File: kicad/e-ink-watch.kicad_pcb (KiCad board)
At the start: 4 copper layers, 40 x 40 mm, 42 parts, among them SW1 BTN1, SW2 BTN2, SW3 BTN3, U1 MDBT50Q-1MV2, U2 BQ25120A

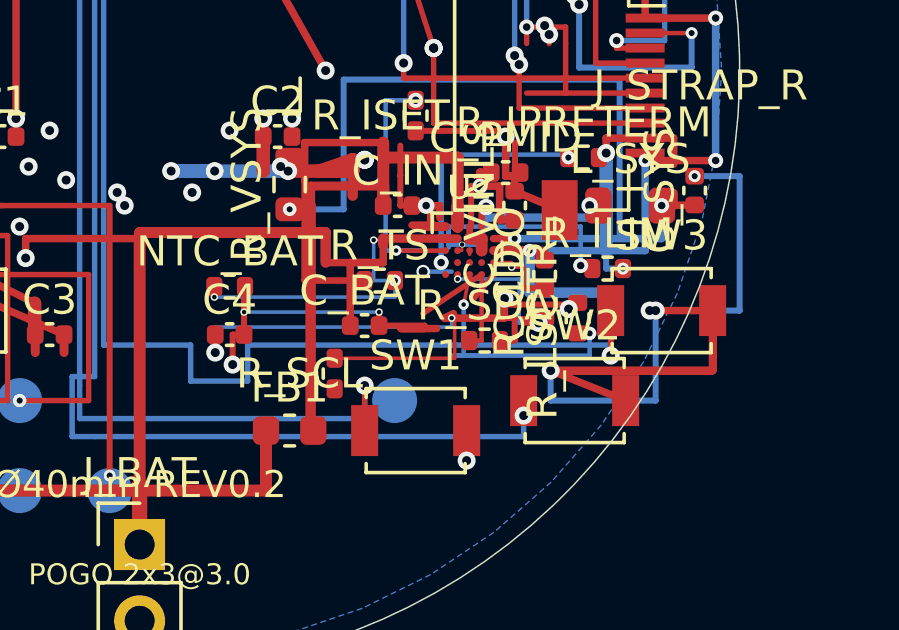
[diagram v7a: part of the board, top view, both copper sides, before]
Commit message: Slide R_SDA north off the SW2 courtyard.
Retract the 3V3 L vertical onto the existing via at x=110.4 so R_SDA can move to y=108.85 without the pad1-vs-3V3 short. Courtyard vs SW2 −0.120 → +0.030. West-of-VBUS SDA hops still hit the TS via drops. Shorting stays 0, unconnected stays 8.

Co-authored-by: illiapliukhin <illiapliukhin@users.noreply.github.com>
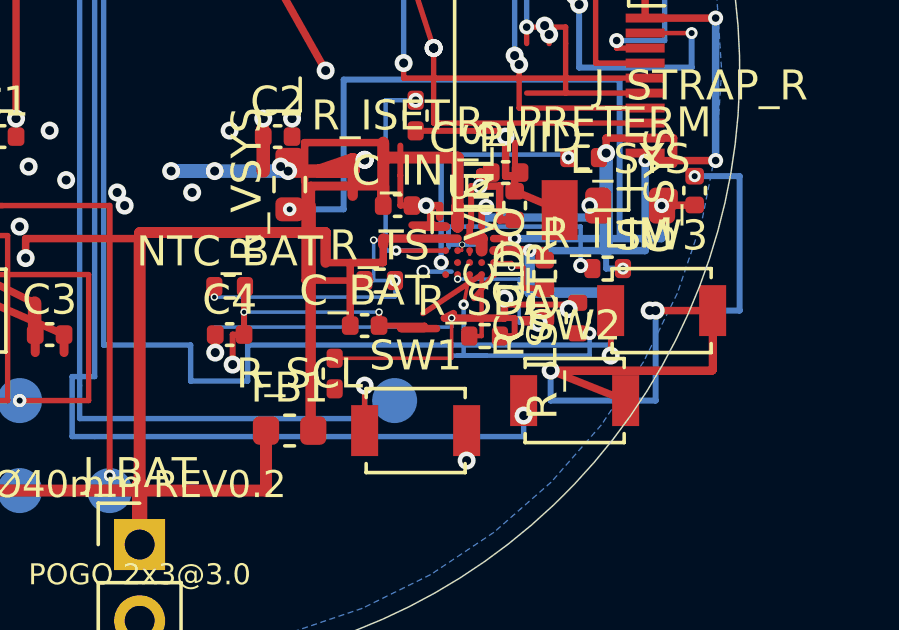
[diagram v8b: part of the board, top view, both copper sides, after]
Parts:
- moved R_SDA 0.15 mm to (111.5, 108.8)
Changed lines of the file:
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@@
 	(footprint "Resistor_SMD:R_0402_1005Metric"
 		(layer "F.Cu")
-		(at 111.5 109.0)
+		(at 111.5 108.85)
 		(descr "Resistor SMD 0402 (1005 Metric), square (rectangular) end terminal, IPC-7351 nominal, (Body size source: IPC-SM-782 page 72, https://www.pcb-3d.com/wordpress/wp-content/uploads/ipc-sm-782a_amendment_1_and_2.pdf), generated with kicad-footprint-generator")
 		(tags "resistor")
@@
 	)
 	(segment
-		(start 110.99 109.0)
-		(end 111.4 109.0)
+		(start 110.99 108.85)
+		(end 111.4 108.85)
 		(width 0.15)
 		(layer "F.Cu")
@@
 	)
 	(segment
-		(start 111.4 109.0)
+		(start 111.4 108.85)
 		(end 111.4 106.8)
 		(width 0.15)
@@
 	)
 	(segment
-		(start 112.01 109.0)
-		(end 112.5 109.0)
+		(start 112.01 108.85)
+		(end 112.5 108.85)
 		(width 0.2)
 		(layer "F.Cu")
@@
 	)
 	(segment
-		(start 112.5 109.0)
+		(start 112.5 108.85)
 		(end 112.5 108.25)
 		(width 0.2)
@@
 	(segment
 		(start 106.5 109.59)
-		(end 110.5 109.59)
+		(end 110.4 109.59)
 		(width 0.12)
 		(layer "F.Cu")
@@
 	)
 	(segment
-		(start 110.5 109.59)
-		(end 110.5 108.25)
+		(start 110.4 109.59)
+		(end 110.4 108.25)
 		(width 0.12)
 		(layer "F.Cu")
@@
 	)
 	(segment
-		(start 110.5 108.25)
+		(start 110.4 108.25)
 		(end 110.16 108.25)
 		(width 0.12)
